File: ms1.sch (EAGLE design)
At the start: 150 parts, among them IC1 MAX3232EUE, IC2 MAX3380EEUP, J1 POWERPOLE_POWER25A, J10 Radio, J11 A3, J12 A4, J13 A5, J14 A6, J15 A7, J16 D1, J17 D2, J18 D3, J19 D4, J2 ON, J20 D5, J21 D6, J22 D7, J3 LED-EN, J4 RS232, J5 RS485, J6 A1, J7 I2C, J8 A2, J9 TTL_SERIAL, Q1 DMG6602SVT, Q2 DMG6602SVT, Q3 DMG6602SVT, Q4 DMG6602SVT, U1 LT1934ES6TRMPBF, U2 LT1934ES6TRMPBF, U3 DS3231SN, U4 ISL3179EIBZ, X1 KUSBVX-BS1N

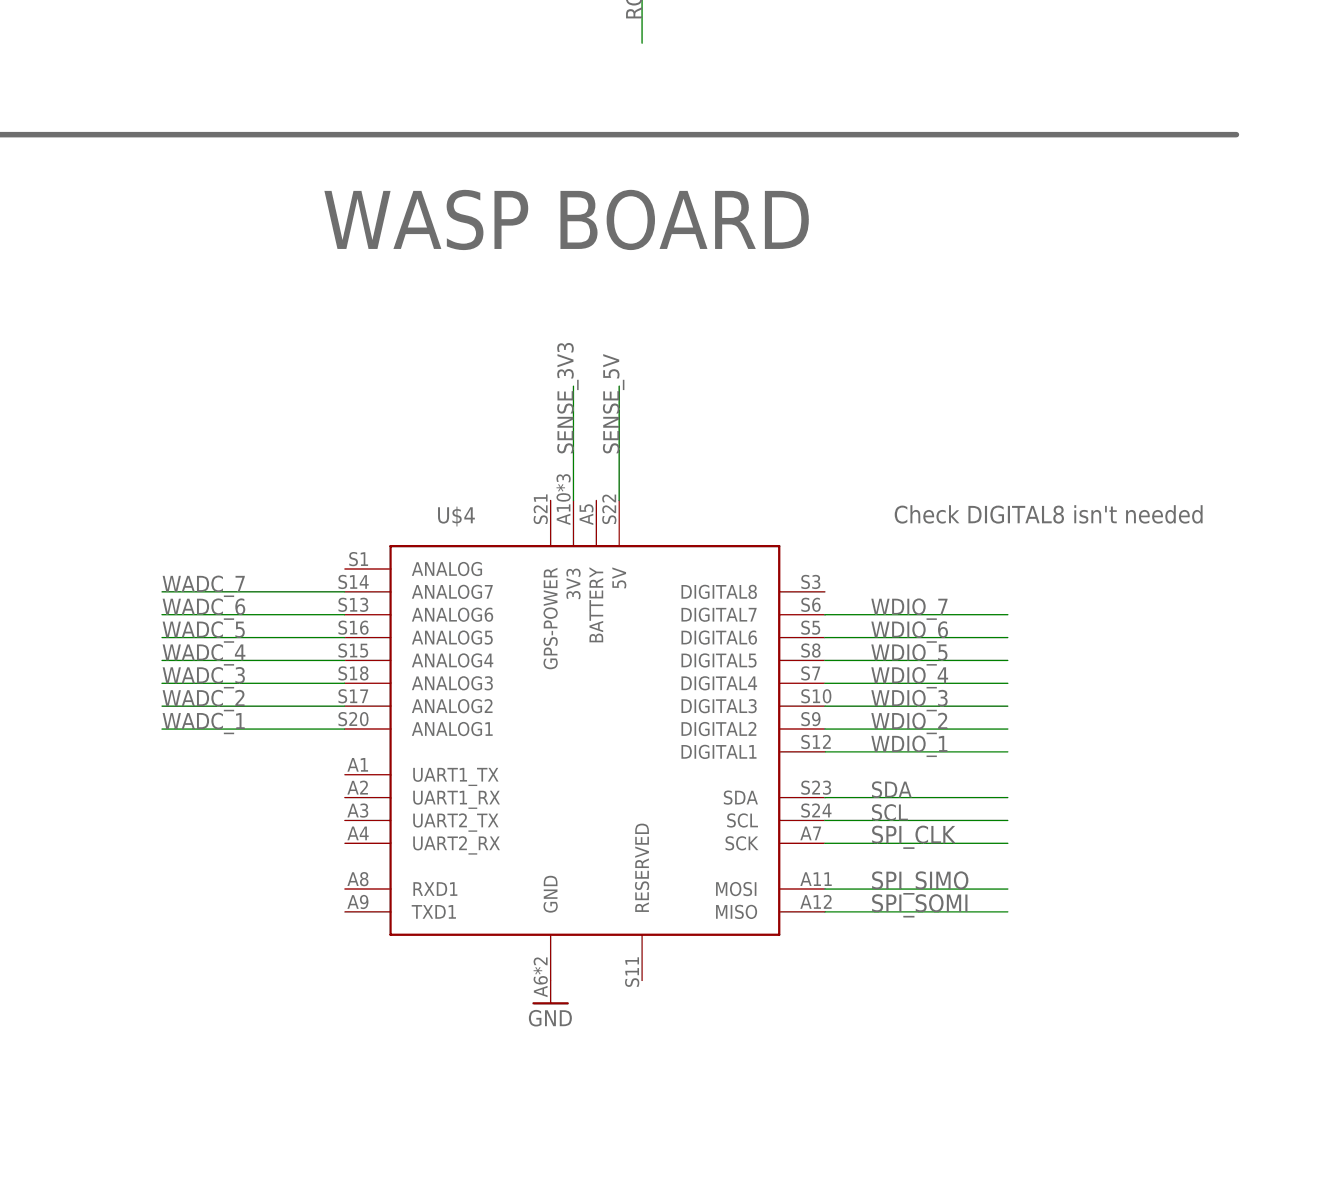
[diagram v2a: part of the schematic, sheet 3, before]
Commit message: removal of libellium part
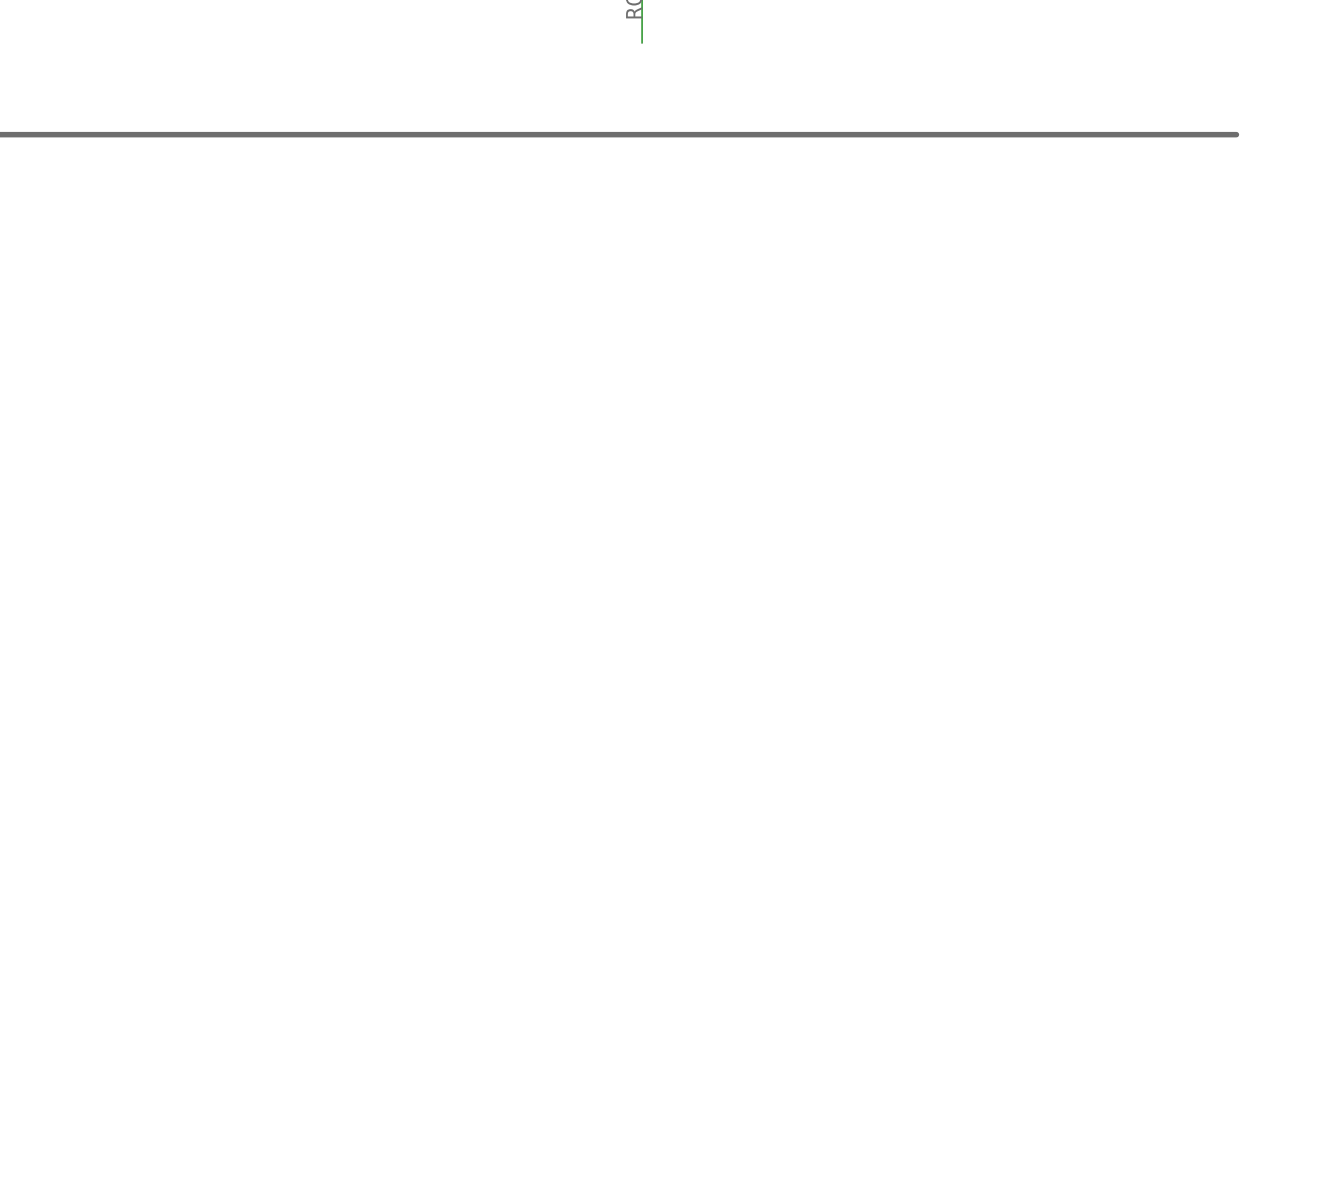
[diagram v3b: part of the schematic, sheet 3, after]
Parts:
- removed U$4: WASP, wasp:WASP
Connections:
- removed net WADC_7: U$4.ANALOG7
- net GND: no longer U$4.GND
- net SCL: no longer U$4.SCL
- net SDA: no longer U$4.SDA
- net SENSE_3V3: no longer U$4.3V3
- net SENSE_5V: no longer U$4.5V
- net SPI_CLK: no longer U$4.SCK
- net SPI_SIMO: no longer U$4.MOSI
- net SPI_SOMI: no longer U$4.MISO
- net WADC_1: no longer U$4.ANALOG1
- net WADC_2: no longer U$4.ANALOG2
- net WADC_3: no longer U$4.ANALOG3
- net WADC_4: no longer U$4.ANALOG4
- net WADC_5: no longer U$4.ANALOG5
- net WADC_6: no longer U$4.ANALOG6
- net WDIO_1: no longer U$4.DIGITAL1
- net WDIO_2: no longer U$4.DIGITAL2
- net WDIO_3: no longer U$4.DIGITAL3
- net WDIO_4: no longer U$4.DIGITAL4
- net WDIO_5: no longer U$4.DIGITAL5
- net WDIO_6: no longer U$4.DIGITAL6
- net WDIO_7: no longer U$4.DIGITAL7
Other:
- note removed: "Check DIGITAL8 isn't needed"
- note removed: "WASP BOARD"
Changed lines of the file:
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@@
 <?xml version="1.0" encoding="utf-8"?>
 <!DOCTYPE eagle SYSTEM "eagle.dtd">
-<eagle version="6.6.0">
+<eagle version="6.5.0">
 <drawing>
 <settings>
@@
 <part name="U$1" library="gumsense" deviceset="BUTTON_CELL_NEW" device=""/>
 <part name="GND5" library="supply1" deviceset="GND" device=""/>
-<part name="U$4" library="wasp" deviceset="WASP" device=""/>
-<part name="GND3" library="supply1" deviceset="GND" device=""/>
 <part name="J7" library="farnell-parts" deviceset="5-PIN-MOLEX" device="" value="I2C"/>
 <part name="GND6" library="supply1" deviceset="GND" device=""/>
@@
 <plain>
 <text x="30.48" y="111.76" size="1.9304" layer="104">ANA0 &amp; ANA7 are attached to dividers on the Z1 to enable 5V input</text>
-<text x="345.44" y="111.76" size="1.9304" layer="95">Check DIGITAL8 isn't needed</text>
 <wire x1="5.08" y1="104.14" x2="144.78" y2="104.14" width="0.6096" layer="95"/>
 <wire x1="144.78" y1="104.14" x2="144.78" y2="45.72" width="0.6096" layer="95"/>
@@
 <text x="294.64" y="243.84" size="6.4516" layer="95">Radio</text>
 <wire x1="241.3" y1="154.94" x2="241.3" y2="45.72" width="0.6096" layer="95"/>
-<text x="281.94" y="142.24" size="6.4516" layer="95">WASP BOARD</text>
 <text x="160.02" y="27.94" size="6.4516" layer="95">BatV / Sense Link</text>
 <wire x1="241.3" y1="45.72" x2="241.3" y2="5.08" width="0.6096" layer="95"/>
@@
 <instance part="GND59" gate="1" x="78.74" y="27.94"/>
 <instance part="C13" gate="G$1" x="58.42" y="45.72" rot="R180"/>
-<instance part="U$4" gate="G$1" x="347.98" y="91.44"/>
-<instance part="GND3" gate="1" x="307.34" y="58.42"/>
 <instance part="U$3" gate="G$1" x="307.34" y="203.2"/>
 <instance part="JP1" gate="A" x="177.8" y="17.78" rot="R90"/>
@@
 </segment>
 <segment>
-<pinref part="U$4" gate="G$1" pin="GND"/>
-<pinref part="GND3" gate="1" pin="GND"/>
-</segment>
-<segment>
 <wire x1="165.1" y1="63.5" x2="165.1" y2="60.96" width="0.1524" layer="91"/>
 <wire x1="170.18" y1="63.5" x2="165.1" y2="63.5" width="0.1524" layer="91"/>
@@
 <label x="93.98" y="195.58" size="1.778" layer="95"/>
 </segment>
-<segment>
-<pinref part="U$4" gate="G$1" pin="SCL"/>
-<wire x1="337.82" y1="78.74" x2="358.14" y2="78.74" width="0.1524" layer="91"/>
-<label x="342.9" y="78.74" size="1.778" layer="95"/>
-</segment>
 </net>
 <net name="SDA" class="0">
@@
 <label x="93.98" y="193.04" size="1.778" layer="95"/>
 </segment>
-<segment>
-<pinref part="U$4" gate="G$1" pin="SDA"/>
-<wire x1="337.82" y1="81.28" x2="358.14" y2="81.28" width="0.1524" layer="91"/>
-<label x="342.9" y="81.28" size="1.778" layer="95"/>
-</segment>
 </net>
 <net name="SPI_CLK" class="0">
@@
 </segment>
 <segment>
-<pinref part="U$4" gate="G$1" pin="SCK"/>
-<wire x1="337.82" y1="76.2" x2="358.14" y2="76.2" width="0.1524" layer="91"/>
-<label x="342.9" y="76.2" size="1.9304" layer="95"/>
-</segment>
-<segment>
 <pinref part="U$3" gate="G$1" pin="SCLK"/>
 <wire x1="289.56" y1="198.12" x2="271.78" y2="198.12" width="0.1524" layer="91"/>
@@
 <label x="271.78" y="208.28" size="1.778" layer="95"/>
 </segment>
-<segment>
-<pinref part="U$4" gate="G$1" pin="MOSI"/>
-<wire x1="337.82" y1="71.12" x2="358.14" y2="71.12" width="0.1524" layer="91"/>
-<label x="342.9" y="71.12" size="1.9304" layer="95"/>
-</segment>
 </net>
 <net name="SPI_SOMI" class="0">
@@
 <wire x1="289.56" y1="203.2" x2="271.78" y2="203.2" width="0.1524" layer="91"/>
 <label x="271.78" y="203.2" size="1.778" layer="95"/>
-</segment>
-<segment>
-<pinref part="U$4" gate="G$1" pin="MISO"/>
-<wire x1="337.82" y1="68.58" x2="358.14" y2="68.58" width="0.1524" layer="91"/>
-<label x="342.9" y="68.58" size="1.9304" layer="95"/>
 </segment>
 </net>
@@
 </net>
 <net name="SENSE_3V3" class="0">
-<segment>
-<pinref part="U$4" gate="G$1" pin="3V3"/>
-<wire x1="309.88" y1="114.3" x2="309.88" y2="127" width="0.1524" layer="91"/>
-<label x="309.88" y="119.38" size="1.778" layer="95" rot="R90"/>
-</segment>
 <segment>
 <wire x1="210.82" y1="76.2" x2="226.06" y2="76.2" width="0.1524" layer="91"/>
@@
 <net name="SENSE_5V" class="0">
 <segment>
-<pinref part="U$4" gate="G$1" pin="5V"/>
-<wire x1="314.96" y1="114.3" x2="314.96" y2="127" width="0.1524" layer="91"/>
-<label x="314.96" y="119.38" size="1.778" layer="95" rot="R90"/>
-</segment>
-<segment>
 <wire x1="210.82" y1="78.74" x2="226.06" y2="78.74" width="0.1524" layer="91"/>
 <label x="210.82" y="78.74" size="1.778" layer="95"/>
@@
 </segment>
 </net>
-<net name="WADC_4" class="0">
-<segment>
-<pinref part="U$4" gate="G$1" pin="ANALOG4"/>
-<wire x1="284.48" y1="96.52" x2="264.16" y2="96.52" width="0.1524" layer="91"/>
-<label x="264.16" y="96.52" size="1.778" layer="95"/>
-</segment>
-</net>
-<net name="WADC_3" class="0">
-<segment>
-<pinref part="U$4" gate="G$1" pin="ANALOG3"/>
-<wire x1="284.48" y1="93.98" x2="264.16" y2="93.98" width="0.1524" layer="91"/>
-<label x="264.16" y="93.98" size="1.778" layer="95"/>
-</segment>
-</net>
-<net name="WADC_2" class="0">
-<segment>
-<pinref part="U$4" gate="G$1" pin="ANALOG2"/>
-<wire x1="284.48" y1="91.44" x2="264.16" y2="91.44" width="0.1524" layer="91"/>
-<label x="264.16" y="91.44" size="1.778" layer="95"/>
-</segment>
-</net>
-<net name="WADC_1" class="0">
-<segment>
-<pinref part="U$4" gate="G$1" pin="ANALOG1"/>
-<wire x1="284.48" y1="88.9" x2="264.16" y2="88.9" width="0.1524" layer="91"/>
-<label x="264.16" y="88.9" size="1.778" layer="95"/>
-</segment>
-</net>
-<net name="WDIO_1" class="0">
-<segment>
-<pinref part="U$4" gate="G$1" pin="DIGITAL1"/>
-<wire x1="337.82" y1="86.36" x2="358.14" y2="86.36" width="0.1524" layer="91"/>
-<label x="342.9" y="86.36" size="1.778" layer="95"/>
-</segment>
-</net>
-<net name="WDIO_2" class="0">
-<segment>
-<pinref part="U$4" gate="G$1" pin="DIGITAL2"/>
-<wire x1="337.82" y1="88.9" x2="358.14" y2="88.9" width="0.1524" layer="91"/>
-<label x="342.9" y="88.9" size="1.778" layer="95"/>
-</segment>
-</net>
-<net name="WDIO_3" class="0">
-<segment>
-<pinref part="U$4" gate="G$1" pin="DIGITAL3"/>
-<wire x1="337.82" y1="91.44" x2="358.14" y2="91.44" width="0.1524" layer="91"/>
-<label x="342.9" y="91.44" size="1.778" layer="95"/>
-</segment>
-</net>
-<net name="WDIO_4" class="0">
-<segment>
-<pinref part="U$4" gate="G$1" pin="DIGITAL4"/>
-<wire x1="337.82" y1="93.98" x2="358.14" y2="93.98" width="0.1524" layer="91"/>
-<label x="342.9" y="93.98" size="1.778" layer="95"/>
-</segment>
-</net>
-<net name="WDIO_5" class="0">
-<segment>
-<pinref part="U$4" gate="G$1" pin="DIGITAL5"/>
-<wire x1="337.82" y1="96.52" x2="358.14" y2="96.52" width="0.1524" layer="91"/>
-<label x="342.9" y="96.52" size="1.778" layer="95"/>
-</segment>
-</net>
-<net name="WDIO_6" class="0">
-<segment>
-<pinref part="U$4" gate="G$1" pin="DIGITAL6"/>
-<wire x1="337.82" y1="99.06" x2="358.14" y2="99.06" width="0.1524" layer="91"/>
-<label x="342.9" y="99.06" size="1.778" layer="95"/>
-</segment>
-</net>
-<net name="WDIO_7" class="0">
-<segment>
-<pinref part="U$4" gate="G$1" pin="DIGITAL7"/>
-<wire x1="337.82" y1="101.6" x2="358.14" y2="101.6" width="0.1524" layer="91"/>
-<label x="342.9" y="101.6" size="1.778" layer="95"/>
-</segment>
-</net>
-<net name="WADC_5" class="0">
-<segment>
-<pinref part="U$4" gate="G$1" pin="ANALOG5"/>
-<wire x1="284.48" y1="99.06" x2="264.16" y2="99.06" width="0.1524" layer="91"/>
-<label x="264.16" y="99.06" size="1.778" layer="95"/>
-</segment>
-</net>
-<net name="WADC_6" class="0">
-<segment>
-<pinref part="U$4" gate="G$1" pin="ANALOG6"/>
-<wire x1="284.48" y1="101.6" x2="264.16" y2="101.6" width="0.1524" layer="91"/>
-<label x="264.16" y="101.6" size="1.778" layer="95"/>
-</segment>
-</net>
-<net name="WADC_7" class="0">
-<segment>
-<pinref part="U$4" gate="G$1" pin="ANALOG7"/>
-<wire x1="284.48" y1="104.14" x2="264.16" y2="104.14" width="0.1524" layer="91"/>
-<label x="264.16" y="104.14" size="1.778" layer="95"/>
-</segment>
-</net>
